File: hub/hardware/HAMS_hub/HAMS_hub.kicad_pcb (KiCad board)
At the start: 2 copper layers, 50.1 x 75 mm, 34 parts, among them J1 Conn_01x06, J10 Conn_01x04, J11 Conn_01x04, J12 Conn_01x04, J2 Conn_01x06, J3 Conn_01x06, J4 Conn_01x06, J5 Conn_01x02, J6 Conn_01x04, J7 Conn_01x04, J8 Conn_01x07, J9 Conn_01x04, Q1 DMG3406L, SW1 TL3305BF100QG, U1 TCA9406DC, U2 NCP5501, U3 NRF24L01_Breakout

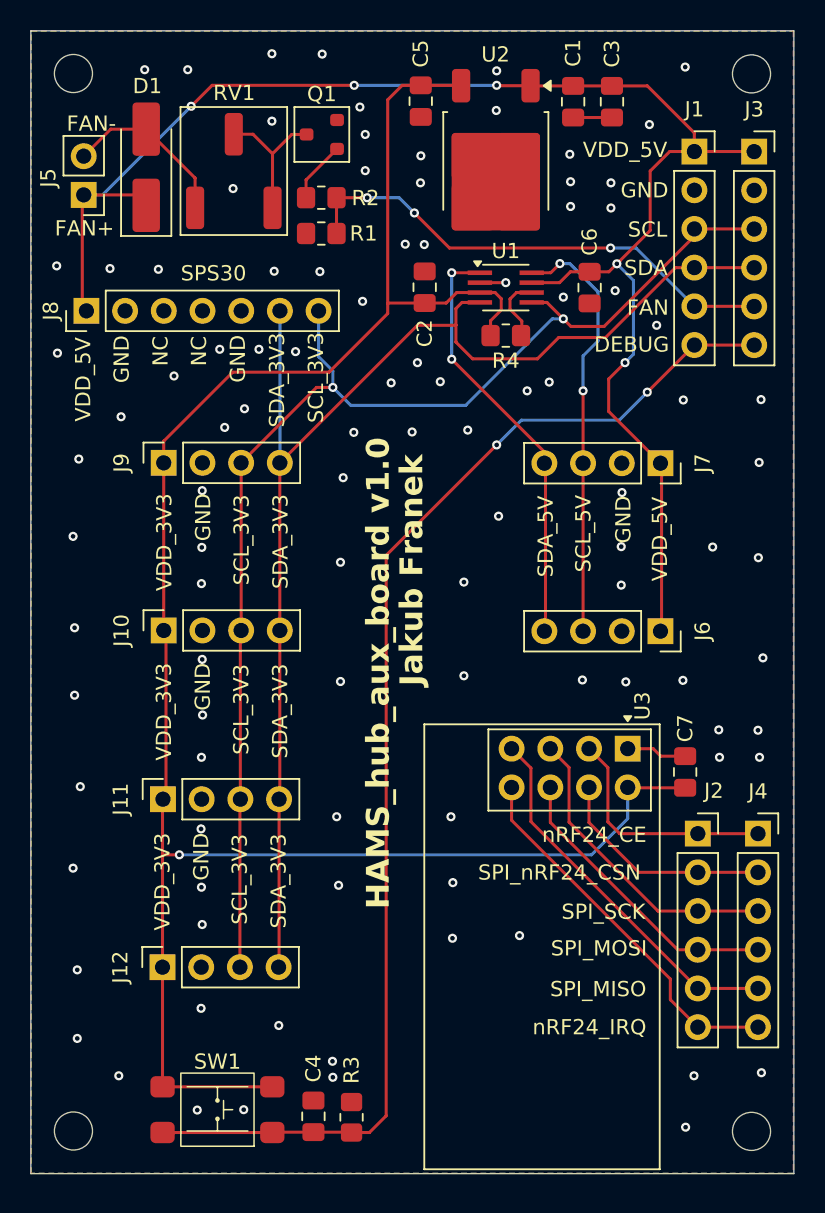
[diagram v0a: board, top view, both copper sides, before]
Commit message: Improve HAMS hub & node HW: schematic and PCB
Finalize hub and node PCB layouts & schematics.
Update task list.
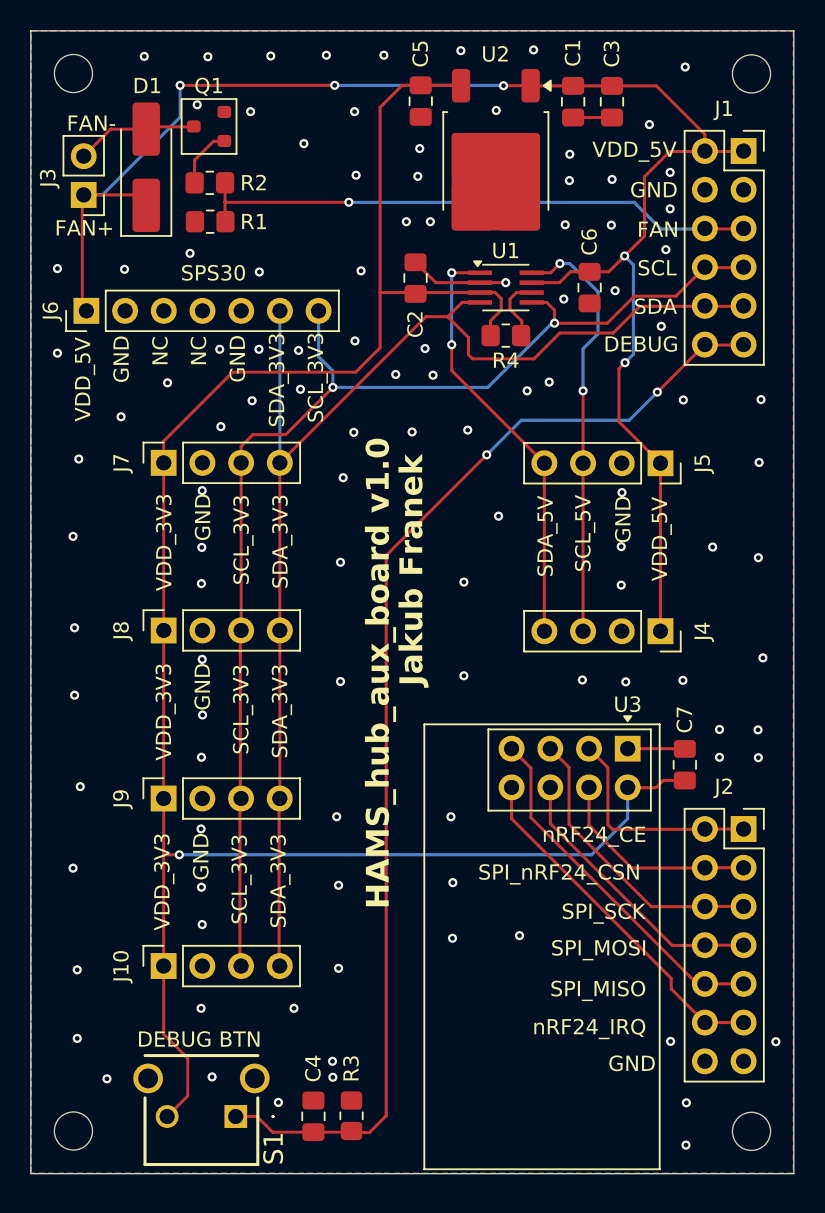
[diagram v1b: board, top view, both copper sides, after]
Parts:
- removed the J3 at (130.9, 66.6)
- removed the J4 at (131.2, 111.4)
- removed RV1: R_Potentiometer_Trim, PCM_Potentiometer_SMD_AKL:Potentiometer_Bourns_3269W_Vertical
- removed SW1: TL3305BF100QG, Personal_Switches:E-Switch_TL3305BF100QG_Tactile_SPST
- added S1: TS11-674-43-BK-260-RA-D, Personal_SamacSys:TS1167443BK260RAD, F.Cu at (96.9, 129.9)
- J1: value Conn_01x06 -> Conn_02x06_Odd_Even; footprint Connector_PinSocket_2.54mm:PinSocket_1x06_P2.54mm_Vertical -> Connector_PinSocket_2.54mm:PinSocket_2x06_P2.54mm_Vertical
- J2: value Conn_01x06 -> Conn_02x07_Odd_Even; footprint Connector_PinSocket_2.54mm:PinSocket_1x06_P2.54mm_Vertical -> Connector_PinSocket_2.54mm:PinSocket_2x07_P2.54mm_Vertical
- moved Q1 7.42 mm to (95.2, 65.0)
- moved R2 7.38 mm to (95.2, 68.7)
- moved R1 7.33 mm to (95.2, 71.2)
- moved J1 3.23 mm to (130.2, 66.6)
- moved J2 3.02 mm to (130.2, 111.1)
- moved C2 0.85 mm to (108.7, 74.9)
- moved C7 0.48 mm to (126.4, 106.9)
- moved J10 0.11 mm to (92.2, 120.1)
- moved R3 0.10 mm to (104.5, 129.9)
- moved J9 0.06 mm to (92.2, 109.1)
- renumbered J12 to J10, J5 to J3, J6 to J4, J7 to J5, J8 to J6, J9 to J7, J10 to J8, J11 to J9
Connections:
- J1 pad 2: GND -> /VDD_5V
- J1 pad 3: /I2C_SCL_3V3 -> GND
- J1 pad 4: /I2C_SDA_3V3 -> GND
- J1 pad 6: /DEBUG_TOGGLE -> /FAN_ON
- J2 pad 2: /SPI_CSN_nRF24 -> /nRF24_CE
- J2 pad 3: /SPI_SCK -> /SPI_CSN_nRF24
- J2 pad 4: /SPI_MOSI -> /SPI_CSN_nRF24
- J2 pad 5: /SPI_MISO -> /SPI_SCK
- J2 pad 6: /nRF24_IRQ -> /SPI_SCK
- Q1 pad 3: Net-(Q1-D) -> Net-(D1-A)
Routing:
- net Net-(Q1-D): track 9.38 -> 0.00 mm
- net /DEBUG_TOGGLE: track 81.8 -> 76.7 mm
- net GND: track 8.23 -> 12.3 mm, vias 103 -> 111
- net /FAN_ON: track 32.7 -> 36.7 mm, vias 3 -> 1
- net /VDD_3V3: track 136.2 -> 132.3 mm
- net Net-(D1-A): track 11.3 -> 7.80 mm
- net /I2C_SCL_3V3: track 83.0 -> 79.8 mm
- net /I2C_SDA_3V3: track 85.8 -> 83.5 mm
- net /SPI_MISO: track 24.7 -> 23.1 mm
- net /nRF24_IRQ: track 24.7 -> 23.2 mm
- net /SPI_MOSI: track 19.4 -> 17.9 mm
- net /SPI_SCK: track 20.1 -> 18.7 mm
- net /SPI_CSN_nRF24: track 14.8 -> 13.3 mm
- net /nRF24_CE: track 15.5 -> 14.0 mm
- net /VDD_5V: track 104.7 -> 105.4 mm
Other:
- board text added: "DEBUG BTN"

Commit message: Improve HAMS hub HW: reset button
Add reset button.
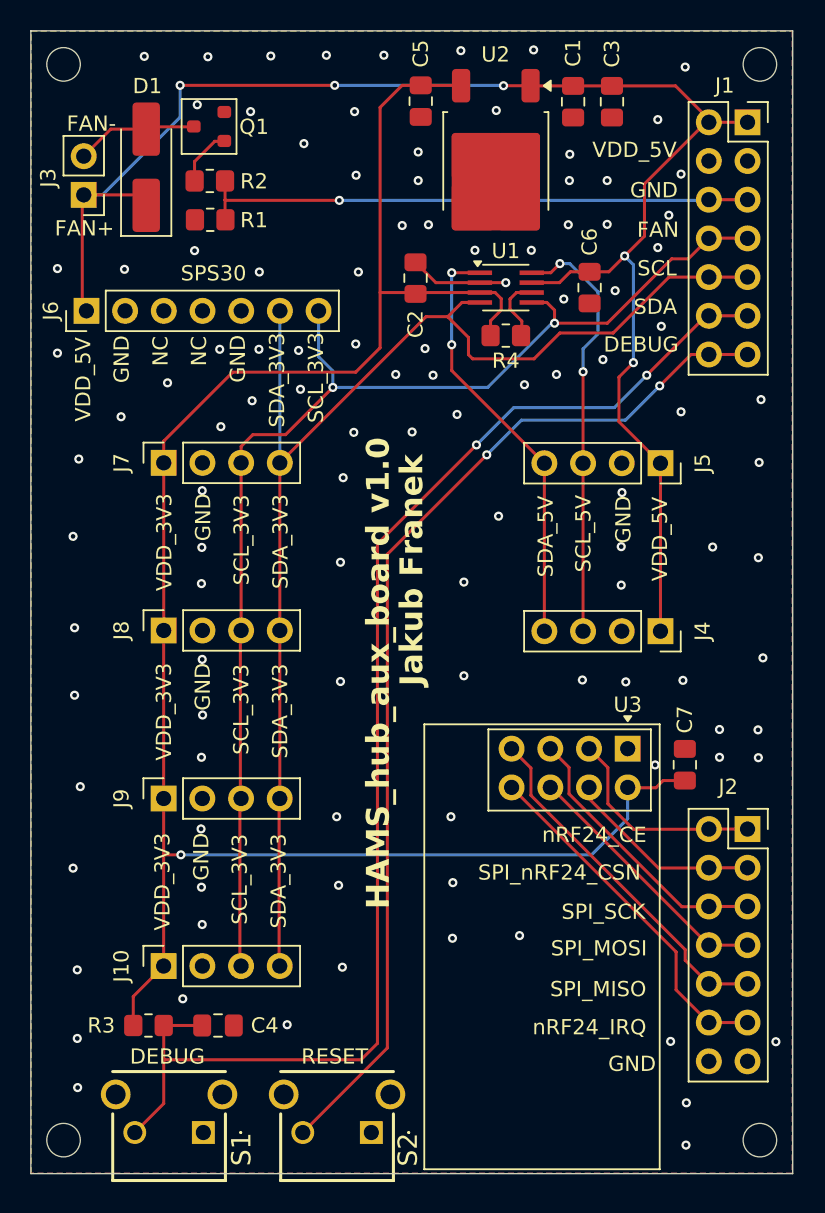
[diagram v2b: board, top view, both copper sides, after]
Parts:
- added S2: TS11-674-43-BK-260-RA-D, Personal_SamacSys:TS1167443BK260RAD, F.Cu at (105.8, 131.0)
- C5: value 4.7 uF -> 4.7 uF, ESR <3 Ohm
- H1, H2, H3, H4: footprint MountingHole:MountingHole_2.5mm -> MountingHole:MountingHole_2.2mm_M2_ISO7380
- J1: value Conn_02x06_Odd_Even -> Conn_02x07_Odd_Even; footprint Connector_PinSocket_2.54mm:PinSocket_2x06_P2.54mm_Vertical -> Connector_PinSocket_2.54mm:PinSocket_2x07_P2.54mm_Vertical
- R2: value 200 -> 100
- moved R3 14.6 mm to (91.2, 124.0), turned to 180 degrees
- moved C4 8.65 mm to (95.7, 124.0), turned to 0 degrees
- moved S1 2.37 mm to (94.8, 131.0)
- moved J1 1.91 mm to (130.5, 64.7)
- moved H4 0.88 mm to (85.6, 60.9)
- moved H3 0.88 mm to (85.6, 131.5)
- moved H1 0.83 mm to (131.3, 60.9)
- moved H2 0.80 mm to (131.3, 131.5)
- moved J2 0.26 mm to (130.5, 111.1)
- moved R1 0.12 mm to (95.2, 71.1)
- moved R2 0.12 mm to (95.2, 68.5)
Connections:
- R3 pad 1: GND -> /DEBUG_TOGGLE
- R3 pad 2: /DEBUG_TOGGLE -> /VDD_3V3
- S1 pad 1: /DEBUG_TOGGLE -> GND
- S1 pad 2: /VDD_3V3 -> /DEBUG_TOGGLE
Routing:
- net /EN: track 0.00 -> 69.6 mm, vias 0 -> 2
- net /DEBUG_TOGGLE: track 76.7 -> 88.1 mm
- net /VDD_3V3: track 132.3 -> 126.0 mm
- net GND: track 12.3 -> 6.52 mm
- net /I2C_SDA_3V3: track 83.5 -> 85.3 mm
- net /I2C_SCL_3V3: track 79.8 -> 81.4 mm
- net /SPI_MOSI: track 17.9 -> 17.2 mm
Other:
- board size 50.1 x 75 mm -> 50 x 75 mm
- board text added: "RESET"
- board text removed: "DEBUG BTN"

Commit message: Improve HAMS node & hub HW: PCB update
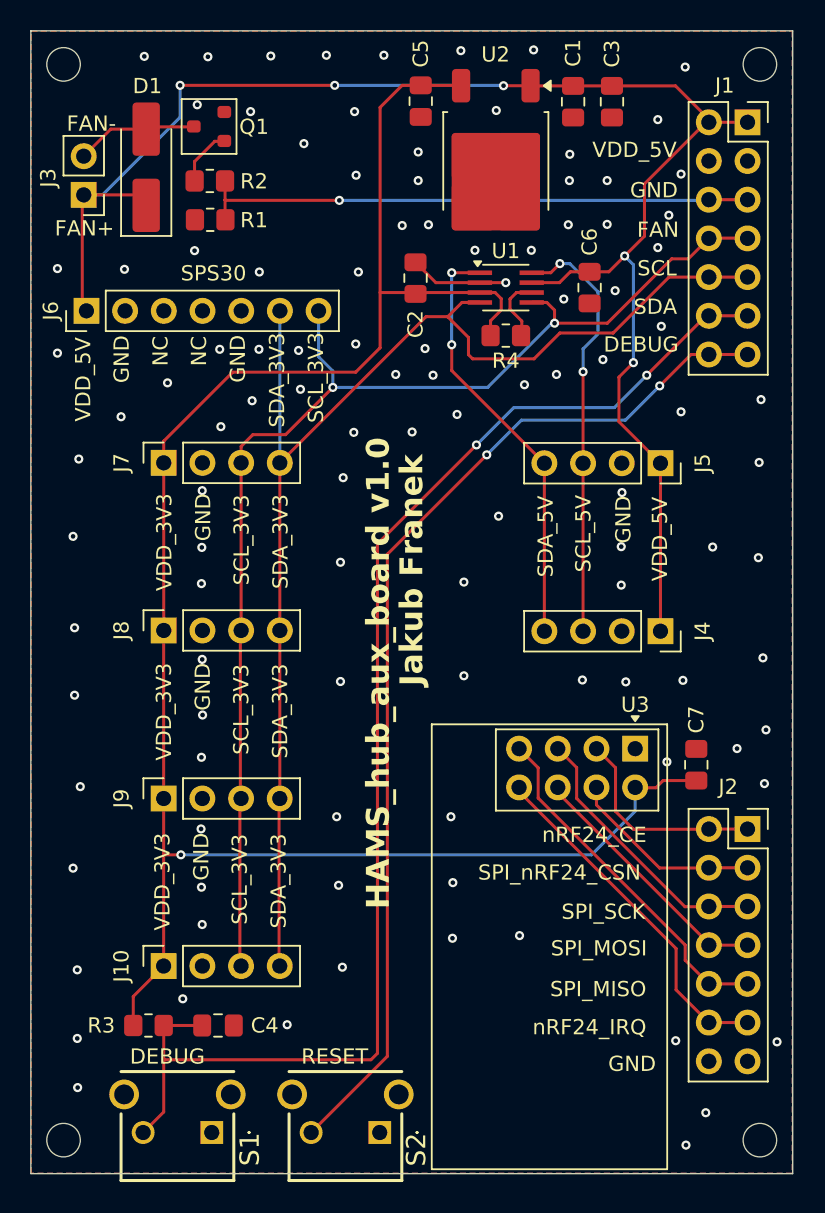
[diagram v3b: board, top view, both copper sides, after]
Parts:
- moved C7 0.75 mm to (127.1, 106.9)
- moved S1 0.55 mm to (95.3, 131.0)
- moved S2 0.55 mm to (106.3, 131.0)
- moved U3 0.49 mm to (123.1, 105.8)
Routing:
- net /VDD_3V3: track 126.0 -> 127.4 mm
- net GND: vias 111 -> 110

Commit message: Improve HAMS node & hub HW: PCB update
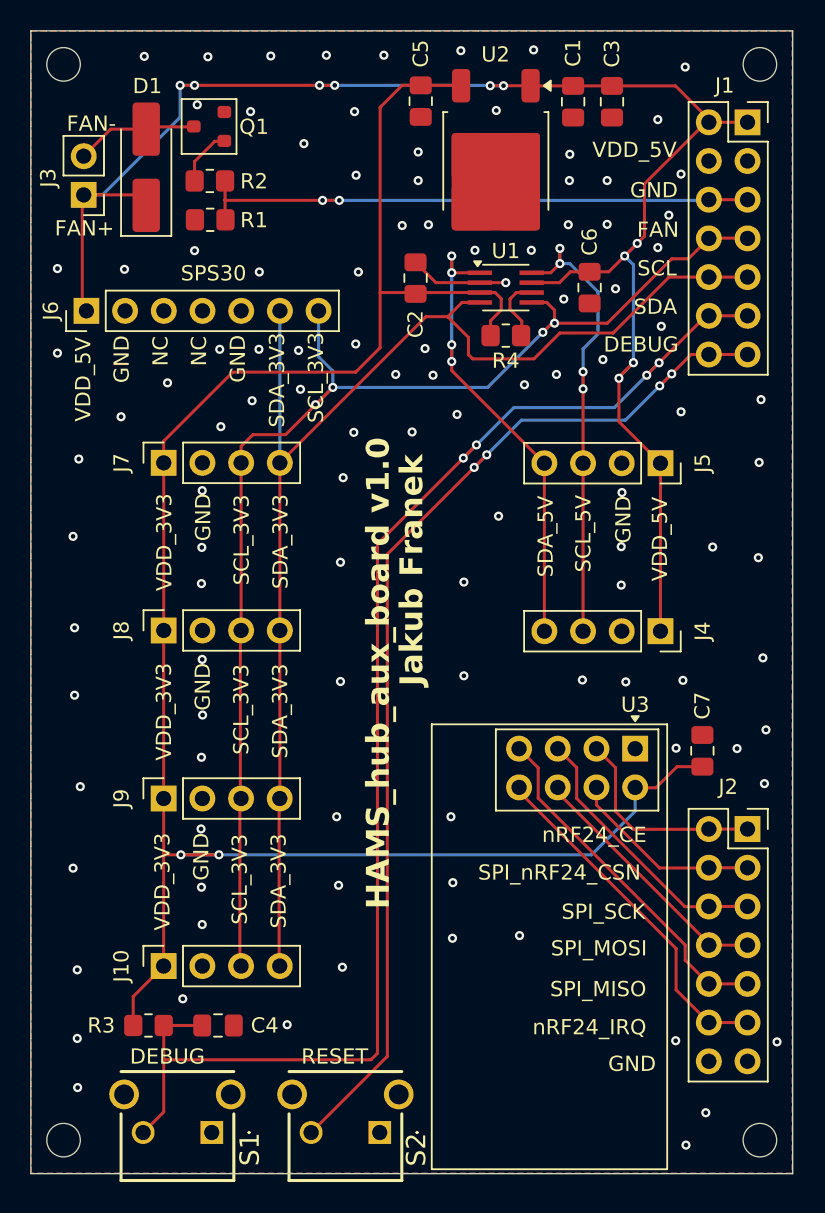
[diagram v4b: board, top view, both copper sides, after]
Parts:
- moved C7 1.00 mm to (127.5, 106.0)
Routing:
- net /VDD_5V: track 105.0 -> 110.4 mm, vias 5 -> 10
- net /I2C_SDA_5V: track 28.0 -> 31.3 mm, vias 2 -> 4
- net /VDD_3V3: track 127.4 -> 130.6 mm, vias 1 -> 2
- net /I2C_SCL_5V: track 28.2 -> 31.3 mm, vias 2 -> 4
- net /I2C_SCL_3V3: track 81.4 -> 84.0 mm, vias 2 -> 4
- net /DEBUG_TOGGLE: track 88.2 -> 90.6 mm, vias 2 -> 4
- net /EN: track 69.4 -> 71.6 mm, vias 2 -> 4
- net /FAN_ON: track 37.0 -> 38.1 mm, vias 1 -> 2
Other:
- board text added: "JLCJLCJLCJLC"
